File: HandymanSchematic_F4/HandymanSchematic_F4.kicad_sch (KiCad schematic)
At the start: 31 parts, among them J1 SWD Header, J2 PWR, J3 JACKS, J4 FOOTSWITCH, J5 ScopeGroundLoop, Q2 2N7002, Q3 2N7002, SW1 RST, SW2 BYP, U3 STM32G030F6P6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

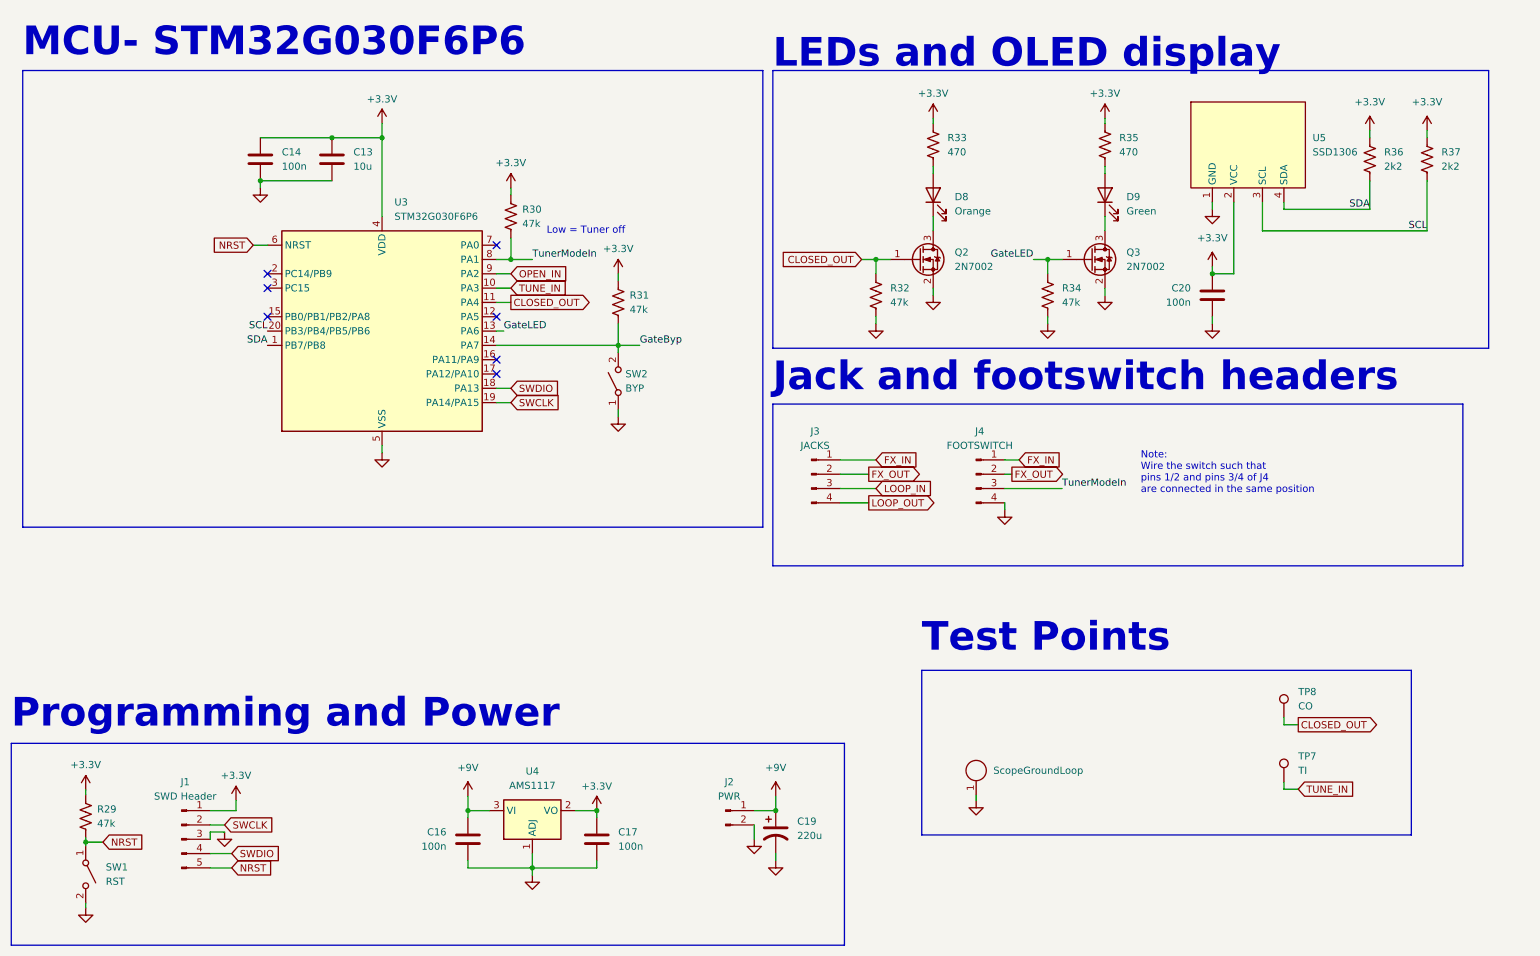
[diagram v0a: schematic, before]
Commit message: attenuator simulation in kicad
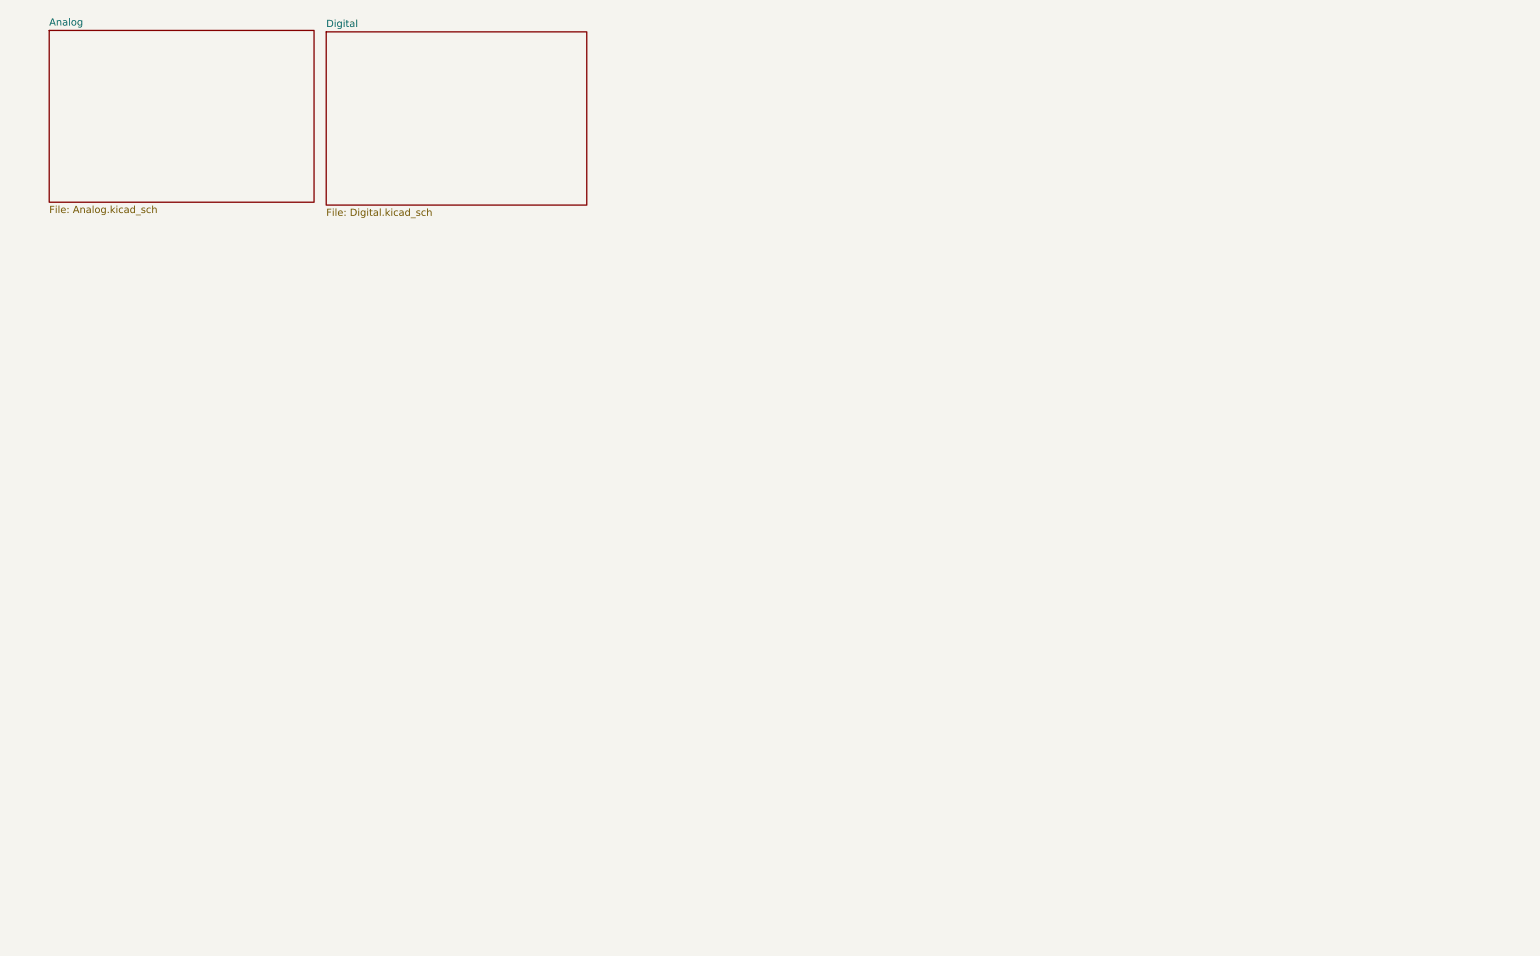
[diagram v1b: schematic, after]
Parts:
- removed C13: 10u, Capacitor_SMD:C_0805_2012Metric, symbol Device:C
- removed C14, C16, C17, C20: 100n, Capacitor_SMD:C_0805_2012Metric, symbol Device:C
- removed C19: 220u, Capacitor_THT:CP_Radial_D5.0mm_P2.50mm, symbol Device:C_Polarized_US
- removed D8: Orange, LED_THT:LED_D3.0mm, symbol Device:LED
- removed D9: Green, LED_THT:LED_D3.0mm, symbol Device:LED
- removed J1: SWD Header, Connector_PinHeader_2.54mm:PinHeader_1x05_P2.54mm_Vertical, symbol Connector:Conn_01x05_Pin
- removed J2: PWR, Connector_PinHeader_2.54mm:PinHeader_1x02_P2.54mm_Vertical, symbol Connector:Conn_01x02_Pin
- removed J3: JACKS, Connector_PinHeader_2.54mm:PinHeader_1x04_P2.54mm_Vertical, symbol Connector:Conn_01x04_Pin
- removed J4: FOOTSWITCH, Connector_PinHeader_2.54mm:PinHeader_1x04_P2.54mm_Vertical, symbol Connector:Conn_01x04_Pin
- removed J5: ScopeGroundLoop, Connector:THT_GND_WIRE, symbol Connector:ScopeGroundLoop
- removed Q2, Q3: 2N7002, Package_TO_SOT_SMD:SOT-23, symbol Transistor_FET:2N7002
- removed R29, R30, R31, R32, R34: 47k, Resistor_SMD:R_0805_2012Metric, symbol Device:R_US
- removed R33, R35: 470, Resistor_SMD:R_0805_2012Metric, symbol Device:R_US
- removed R36, R37: 2k2, Resistor_SMD:R_0805_2012Metric, symbol Device:R_US
- removed SW1: RST, Button_Switch_SMD:SW_SPST_B3U-1000P, symbol Switch:SW_SPST
- removed SW2: BYP, Button_Switch_THT:MiniToggle_SPST, symbol Switch:SW_SPST
- removed TP7: TI, TestPoint:TestPoint_THTPad_D2.0mm_Drill1.0mm_VAL, symbol Connector:TestPoint
- removed TP8: CO, TestPoint:TestPoint_THTPad_D2.0mm_Drill1.0mm_VAL, symbol Connector:TestPoint
- removed U3: STM32G030F6P6, Package_SO:TSSOP-20_4.4x6.5mm_P0.65mm, symbol MCU_ST_STM32G0:STM32G030F6Px
- removed U4: AMS1117, Package_TO_SOT_SMD:SOT-223-3_TabPin2, symbol Regulator_Linear:AMS1117
- removed U5: SSD1306, Display:SSD1306_OLED_128x64_OffBoard, symbol Display_Graphic:SSD1306_OLED_128x64
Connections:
- no-connect marks 7 -> 0
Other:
- added sheet Analog (Analog.kicad_sch)
- added sheet Digital (Digital.kicad_sch)
- note removed: "Jack and footswitch headers"
- note removed: "LEDs and OLED display"
- note removed: "Low = Tuner off"
- note removed: "MCU- STM32G030F6P6"
- note removed: "Note: Wire the switch such that pins 1/2 and pins 3/4 of J4 are connected in the same position"
- note removed: "Programming and Power"
- note removed: "Test Points"
